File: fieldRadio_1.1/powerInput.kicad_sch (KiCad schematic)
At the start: 7 parts, among them Q21 IRF9540, U10 LM1086-5.0

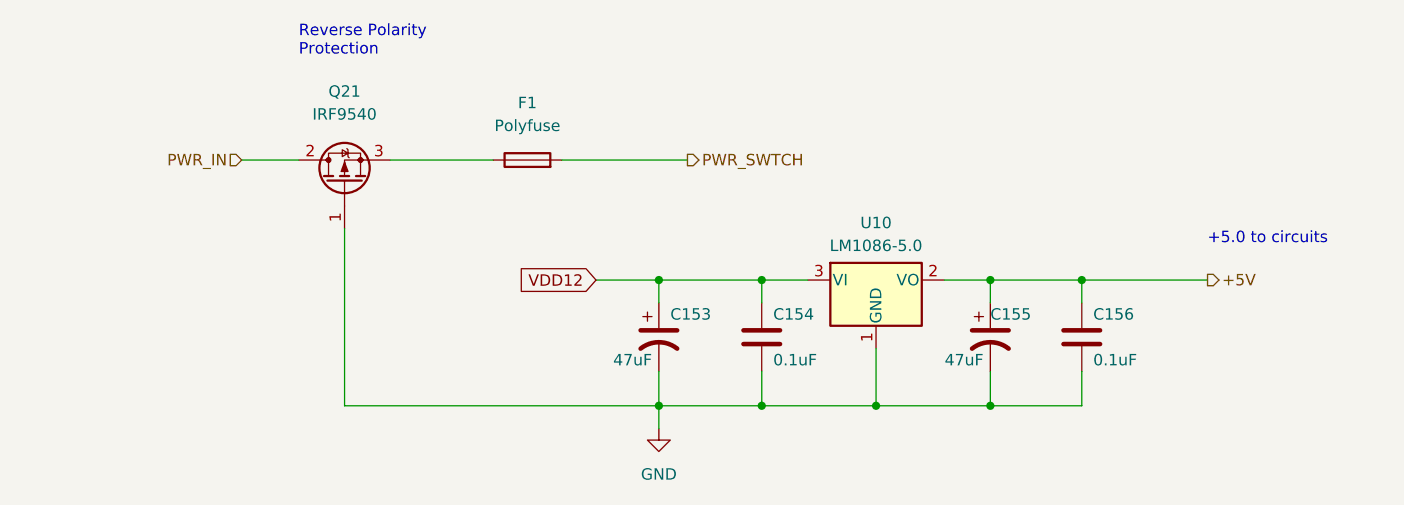
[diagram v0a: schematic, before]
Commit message: Added PTT and TP for clocks
More layout cleanup and tuning.
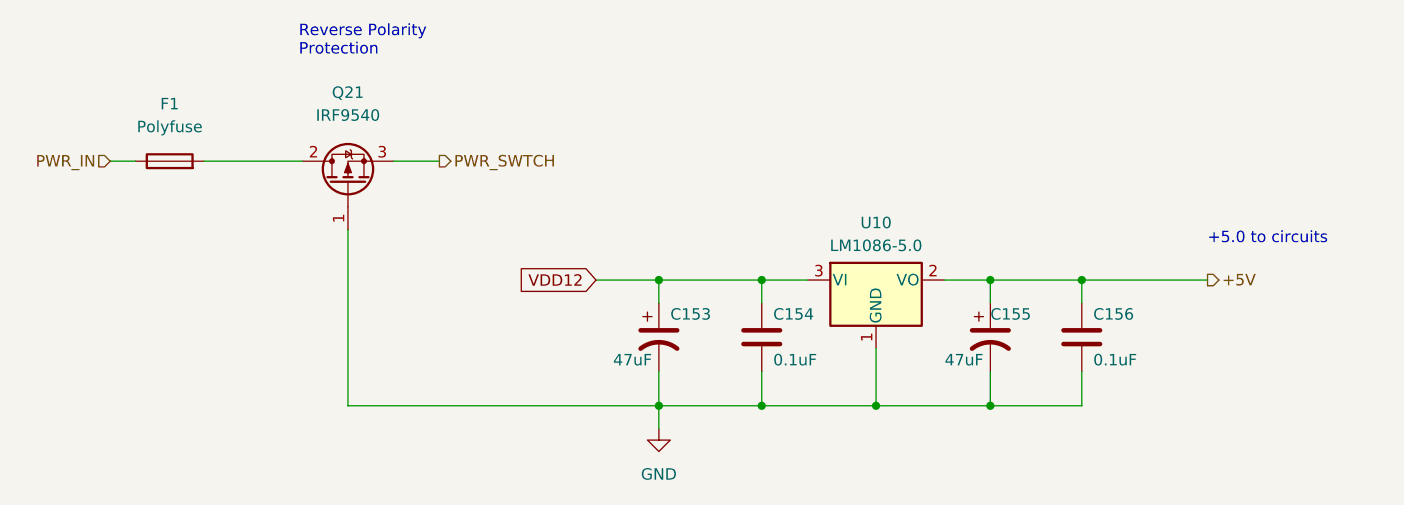
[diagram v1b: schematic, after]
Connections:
- net PWR_IN: now also F1.1; no longer Q21.2 (D)
- net PWR_SWTCH: now also Q21.3 (S); no longer F1.2
- new net: F1.2, Q21.2 (D)
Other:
- moved on the sheet: F1
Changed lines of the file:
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@@
     (stroke (width 0) (type default))
   )
-  (wire (pts (xy 173.355 153.67) (xy 208.28 153.67))
+  (wire (pts (xy 173.736 153.67) (xy 208.28 153.67))
     (stroke (width 0) (type default))
   )
@@
     (stroke (width 0) (type default))
   )
-  (wire (pts (xy 178.435 126.365) (xy 189.865 126.365))
-    (stroke (width 0) (type default))
-  )
   (wire (pts (xy 219.71 149.86) (xy 219.71 153.67))
     (stroke (width 0) (type default))
@@
     (stroke (width 0) (type default))
   )
-  (wire (pts (xy 173.355 133.985) (xy 173.355 153.67))
+  (wire (pts (xy 173.736 134.112) (xy 173.736 153.67))
     (stroke (width 0) (type default))
   )
@@
     (stroke (width 0) (type default))
   )
+  (wire (pts (xy 157.734 126.492) (xy 168.656 126.492))
+    (stroke (width 0) (type default))
+  )
   (wire (pts (xy 245.11 139.7) (xy 245.11 142.24))
     (stroke (width 0) (type default))
   )
-  (wire (pts (xy 161.925 126.365) (xy 168.275 126.365))
+  (wire (pts (xy 147.32 126.492) (xy 150.114 126.492))
     (stroke (width 0) (type default))
   )
@@
     (stroke (width 0) (type default))
   )
-  (wire (pts (xy 197.485 126.365) (xy 211.455 126.365))
+  (wire (pts (xy 178.816 126.492) (xy 183.896 126.492))
     (stroke (width 0) (type default))
   )
@@
     )
   )
-  (hierarchical_label "PWR_IN" (shape input) (at 161.925 126.365 180) (fields_autoplaced)
+  (hierarchical_label "PWR_IN" (shape input) (at 147.32 126.492 180) (fields_autoplaced)
     (effects (font (size 1.27 1.27)) (justify right))
   )
@@
     (effects (font (size 1.27 1.27)) (justify left))
   )
-  (hierarchical_label "PWR_SWTCH" (shape output) (at 211.455 126.365 0) (fields_autoplaced)
+  (hierarchical_label "PWR_SWTCH" (shape output) (at 183.896 126.492 0) (fields_autoplaced)
     (effects (font (size 1.27 1.27)) (justify left))
   )
@@
     )
   )
-  (symbol (lib_id "Device:Q_PMOS_GDS") (at 173.355 128.905 90) (unit 1)
+  (symbol (lib_id "Device:Q_PMOS_GDS") (at 173.736 129.032 90) (unit 1)
     (in_bom yes) (on_board yes) (dnp no) (fields_autoplaced)
-    (property "Reference" "Q21" (at 173.355 118.745 90)
-      (effects (font (size 1.27 1.27)))
-    )
-    (property "Value" "IRF9540" (at 173.355 121.285 90)
-      (effects (font (size 1.27 1.27)))
-    )
-    (property "Footprint" "Package_TO_SOT_THT:TO-220-3_Vertical" (at 170.815 123.825 0)
-      (effects (font (size 1.27 1.27)) hide)
-    )
-    (property "Datasheet" "~" (at 173.355 128.905 0)
+    (property "Reference" "Q21" (at 173.736 118.872 90)
+      (effects (font (size 1.27 1.27)))
+    )
+    (property "Value" "IRF9540" (at 173.736 121.412 90)
+      (effects (font (size 1.27 1.27)))
+    )
+    (property "Footprint" "Package_TO_SOT_THT:TO-220-3_Vertical" (at 171.196 123.952 0)
+      (effects (font (size 1.27 1.27)) hide)
+    )
+    (property "Datasheet" "~" (at 173.736 129.032 0)
       (effects (font (size 1.27 1.27)) hide)
     )
@@
     )
   )
-  (symbol (lib_id "Device:Fuse") (at 193.675 126.365 90) (unit 1)
+  (symbol (lib_id "Device:Fuse") (at 153.924 126.492 90) (unit 1)
     (in_bom yes) (on_board yes) (dnp no) (fields_autoplaced)
-    (property "Reference" "F1" (at 193.675 120.015 90)
-      (effects (font (size 1.27 1.27)))
-    )
-    (property "Value" "Polyfuse" (at 193.675 122.555 90)
-      (effects (font (size 1.27 1.27)))
-    )
-    (property "Footprint" "Fuse:Fuse_2920_7451Metric_Pad2.10x5.45mm_HandSolder" (at 193.675 128.143 90)
-      (effects (font (size 1.27 1.27)) hide)
-    )
-    (property "Datasheet" "~" (at 193.675 126.365 0)
-      (effects (font (size 1.27 1.27)) hide)
-    )
+    (property "Reference" "F1" (at 153.924 120.142 90)
+      (effects (font (size 1.27 1.27)))
+    )
+    (property "Value" "Polyfuse" (at 153.924 122.682 90)
+      (effects (font (size 1.27 1.27)))
+    )
+    (property "Footprint" "Fuse:Fuse_2920_7451Metric_Pad2.10x5.45mm_HandSolder" (at 153.924 128.27 90)
+      (effects (font (size 1.27 1.27)) hide)
+    )
+    (property "Datasheet" "~" (at 153.924 126.492 0)
+      (effects (font (size 1.27 1.27)) hide)
+    )
